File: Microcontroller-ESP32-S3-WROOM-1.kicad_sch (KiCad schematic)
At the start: 26 parts, among them Q1 BC817, Q2 BC817, U1 ESP32-S3-WROOM-1, U4 CP2102N-Axx-xQFN20

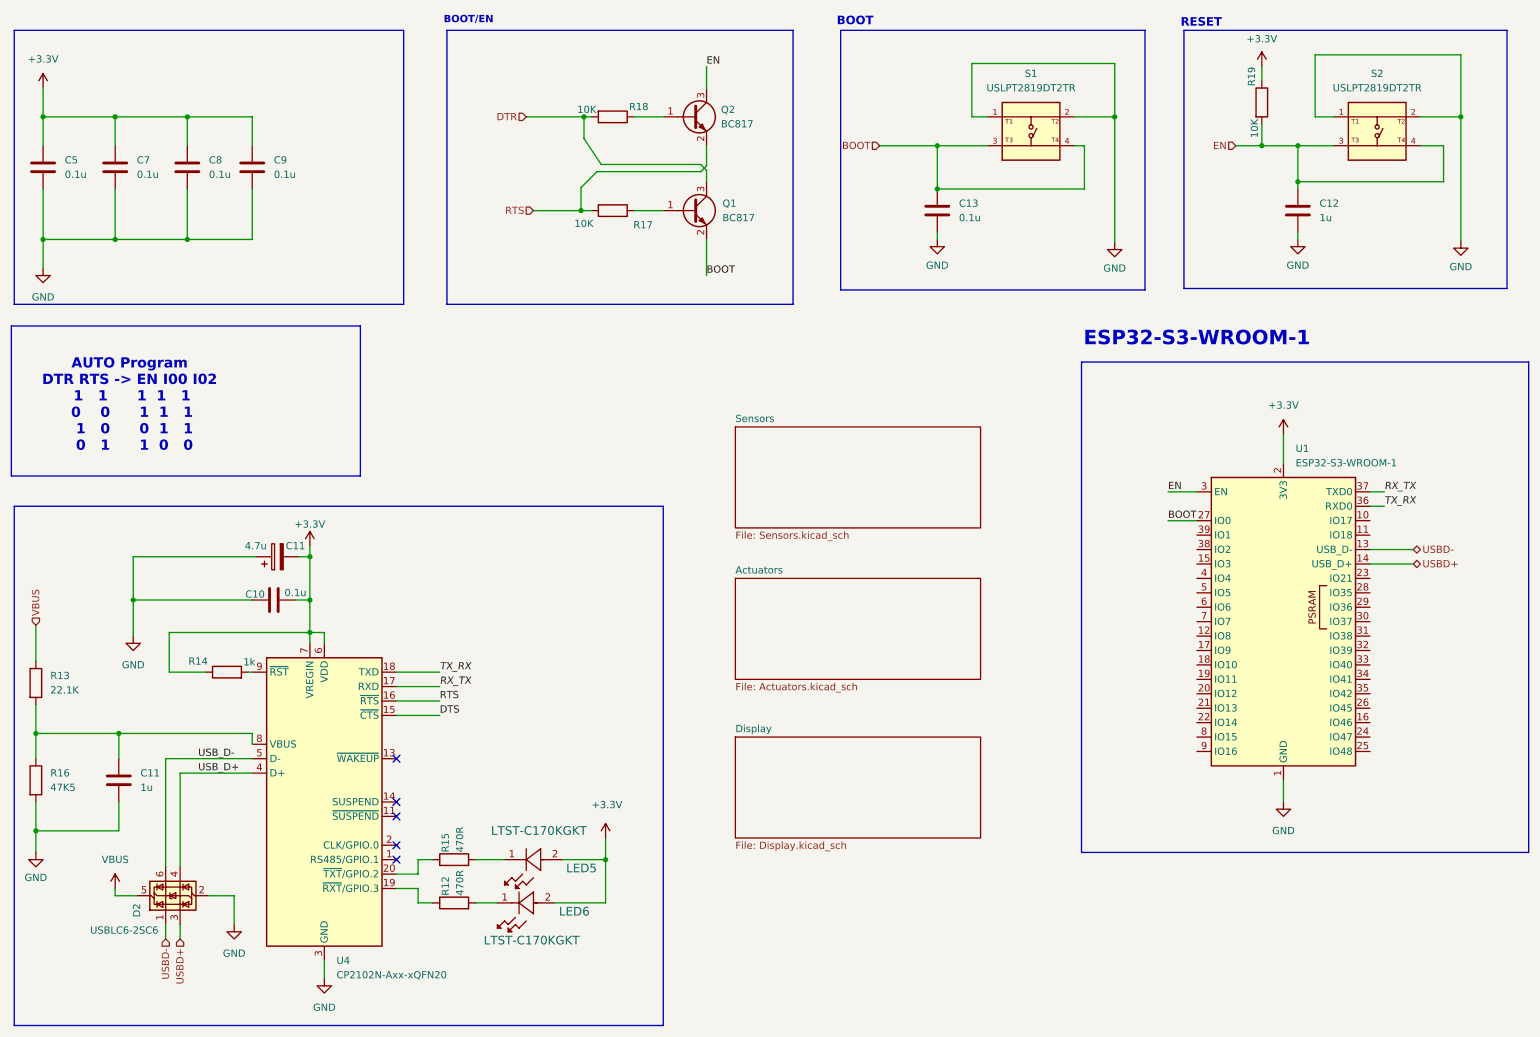
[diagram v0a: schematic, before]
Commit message: feat(hw): update component references for improved consistency in PCB design
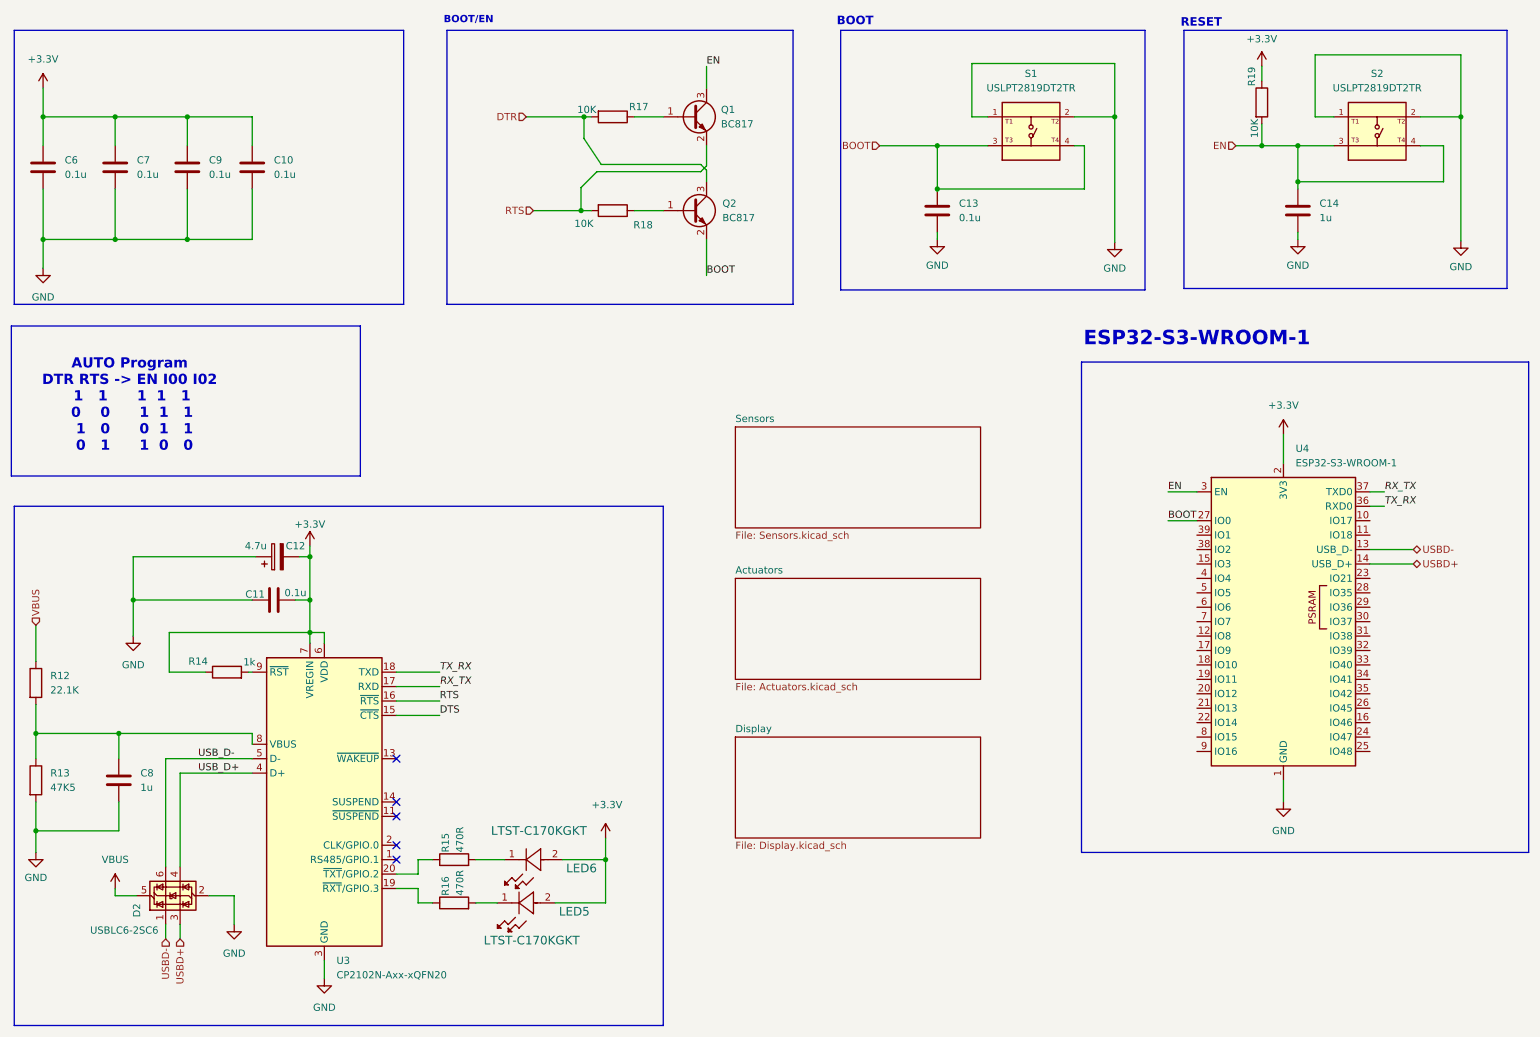
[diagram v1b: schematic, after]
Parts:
- renumbered C9 to C10, C10 to C11, C11 to C12, C12 to C14, C5 to C6, C11 to C8, C8 to C9, LED6 to LED5, LED5 to LED6, Q2 to Q1, Q1 to Q2, R13 to R12, R16 to R13, R12 to R16, R18 to R17, R17 to R18, U4 to U3, U1 to U4
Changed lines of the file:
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@@
 		(dnp no)
 		(fields_autoplaced yes)
-		(property "Reference" "Q1"
+		(property "Reference" "Q2"
 			(at 139.954 48.2599 0)
 			(effects
@@
 			(project "iot_device_pcb"
 				(path "/20a6db8f-6f9d-426b-a90e-3cd30ac36ee8/d76e5a61-e019-4441-8e0f-87cbb4ce42a5"
-					(reference "Q1")
+					(reference "Q2")
 					(unit 1)
 				)
@@
 		(dnp no)
 		(fields_autoplaced yes)
-		(property "Reference" "#PWR025"
+		(property "Reference" "#PWR039"
 			(at 238.76 92.71 0)
 			(effects
@@
 			(project ""
 				(path "/20a6db8f-6f9d-426b-a90e-3cd30ac36ee8/d76e5a61-e019-4441-8e0f-87cbb4ce42a5"
-					(reference "#PWR025")
+					(reference "#PWR039")
 					(unit 1)
 				)
@@
 		(dnp no)
 		(fields_autoplaced yes)
-		(property "Reference" "C9"
+		(property "Reference" "C10"
 			(at 60.96 40.6399 0)
 			(effects
@@
 			(project "iot_device_pcb"
 				(path "/20a6db8f-6f9d-426b-a90e-3cd30ac36ee8/d76e5a61-e019-4441-8e0f-87cbb4ce42a5"
-					(reference "C9")
+					(reference "C10")
 					(unit 1)
 				)
@@
 		(dnp no)
 		(fields_autoplaced yes)
-		(property "Reference" "#PWR0107"
+		(property "Reference" "#PWR036"
 			(at 177.8 60.96 0)
 			(effects
@@
 			(project "iot_device_pcb"
 				(path "/20a6db8f-6f9d-426b-a90e-3cd30ac36ee8/d76e5a61-e019-4441-8e0f-87cbb4ce42a5"
-					(reference "#PWR0107")
+					(reference "#PWR036")
 					(unit 1)
 				)
@@
 		(on_board yes)
 		(dnp no)
-		(property "Reference" "LED6"
+		(property "Reference" "LED5"
 			(at 116.586 172.974 0)
 			(effects
@@
 			(project "iot_device_pcb"
 				(path "/20a6db8f-6f9d-426b-a90e-3cd30ac36ee8/d76e5a61-e019-4441-8e0f-87cbb4ce42a5"
-					(reference "LED6")
+					(reference "LED5")
 					(unit 1)
 				)
@@
 		(dnp no)
 		(fields_autoplaced yes)
-		(property "Reference" "#PWR027"
+		(property "Reference" "#PWR028"
 			(at 20.32 31.75 0)
 			(effects
@@
 			(project "iot_device_pcb"
 				(path "/20a6db8f-6f9d-426b-a90e-3cd30ac36ee8/d76e5a61-e019-4441-8e0f-87cbb4ce42a5"
-					(reference "#PWR027")
+					(reference "#PWR028")
 					(unit 1)
 				)
@@
 		(dnp no)
 		(fields_autoplaced yes)
-		(property "Reference" "R13"
+		(property "Reference" "R12"
 			(at 21.59 131.4449 0)
 			(effects
@@
 			(project "iot_device_pcb"
 				(path "/20a6db8f-6f9d-426b-a90e-3cd30ac36ee8/d76e5a61-e019-4441-8e0f-87cbb4ce42a5"
-					(reference "R13")
+					(reference "R12")
 					(unit 1)
 				)
@@
 		(dnp no)
 		(fields_autoplaced yes)
-		(property "Reference" "C12"
+		(property "Reference" "C14"
 			(at 245.11 48.2599 0)
 			(effects
@@
 			(project "iot_device_pcb"
 				(path "/20a6db8f-6f9d-426b-a90e-3cd30ac36ee8/d76e5a61-e019-4441-8e0f-87cbb4ce42a5"
-					(reference "C12")
+					(reference "C14")
 					(unit 1)
 				)
@@
 		(dnp no)
 		(fields_autoplaced yes)
-		(property "Reference" "R16"
+		(property "Reference" "R13"
 			(at 21.59 148.5899 0)
 			(effects
@@
 			(project "iot_device_pcb"
 				(path "/20a6db8f-6f9d-426b-a90e-3cd30ac36ee8/d76e5a61-e019-4441-8e0f-87cbb4ce42a5"
-					(reference "R16")
+					(reference "R13")
 					(unit 1)
 				)
@@
 		(dnp no)
 		(fields_autoplaced yes)
-		(property "Reference" "#PWR0104"
+		(property "Reference" "#PWR041"
 			(at 241.3 60.96 0)
 			(effects
@@
 			(project "iot_device_pcb"
 				(path "/20a6db8f-6f9d-426b-a90e-3cd30ac36ee8/d76e5a61-e019-4441-8e0f-87cbb4ce42a5"
-					(reference "#PWR0104")
+					(reference "#PWR041")
 					(unit 1)
 				)
@@
 		(dnp no)
 		(fields_autoplaced yes)
-		(property "Reference" "U4"
+		(property "Reference" "U3"
 			(at 71.9933 181.61 0)
 			(effects
@@
 			(project "iot_device_pcb"
 				(path "/20a6db8f-6f9d-426b-a90e-3cd30ac36ee8/d76e5a61-e019-4441-8e0f-87cbb4ce42a5"
-					(reference "U4")
+					(reference "U3")
 					(unit 1)
 				)
@@
 		(on_board yes)
 		(dnp no)
-		(property "Reference" "R18"
+		(property "Reference" "R17"
 			(at 125.222 31.242 90)
 			(effects
@@
 			(project "iot_device_pcb"
 				(path "/20a6db8f-6f9d-426b-a90e-3cd30ac36ee8/d76e5a61-e019-4441-8e0f-87cbb4ce42a5"
-					(reference "R18")
+					(reference "R17")
 					(unit 1)
 				)
@@
 		(on_board yes)
 		(dnp no)
-		(property "Reference" "R17"
+		(property "Reference" "R18"
 			(at 125.984 52.07 90)
 			(effects
@@
 			(project "iot_device_pcb"
 				(path "/20a6db8f-6f9d-426b-a90e-3cd30ac36ee8/d76e5a61-e019-4441-8e0f-87cbb4ce42a5"
-					(reference "R17")
+					(reference "R18")
 					(unit 1)
 				)
@@
 		(on_board yes)
 		(dnp no)
-		(property "Reference" "LED5"
+		(property "Reference" "LED6"
 			(at 117.856 165.354 0)
 			(effects
@@
 			(project "iot_device_pcb"
 				(path "/20a6db8f-6f9d-426b-a90e-3cd30ac36ee8/d76e5a61-e019-4441-8e0f-87cbb4ce42a5"
-					(reference "LED5")
+					(reference "LED6")
 					(unit 1)
 				)
@@
 		(dnp no)
 		(fields_autoplaced yes)
-		(property "Reference" "U1"
+		(property "Reference" "U4"
 			(at 240.9033 91.44 0)
 			(effects
@@
 			(project ""
 				(path "/20a6db8f-6f9d-426b-a90e-3cd30ac36ee8/d76e5a61-e019-4441-8e0f-87cbb4ce42a5"
-					(reference "U1")
+					(reference "U4")
 					(unit 1)
 				)
@@
 		(dnp no)
 		(fields_autoplaced yes)
-		(property "Reference" "#PWR0106"
+		(property "Reference" "#PWR038"
 			(at 234.95 27.94 0)
 			(effects
@@
 			(project "iot_device_pcb"
 				(path "/20a6db8f-6f9d-426b-a90e-3cd30ac36ee8/d76e5a61-e019-4441-8e0f-87cbb4ce42a5"
-					(reference "#PWR0106")
+					(reference "#PWR038")
 					(unit 1)
 				)
@@
 		(dnp no)
 		(fields_autoplaced yes)
-		(property "Reference" "C5"
+		(property "Reference" "C6"
 			(at 24.13 40.6399 0)
 			(effects
@@
 			(project "iot_device_pcb"
 				(path "/20a6db8f-6f9d-426b-a90e-3cd30ac36ee8/d76e5a61-e019-4441-8e0f-87cbb4ce42a5"
-					(reference "C5")
+					(reference "C6")
 					(unit 1)
 				)
@@
 		(dnp no)
 		(fields_autoplaced yes)
-		(property "Reference" "#PWR028"
+		(property "Reference" "#PWR030"
 			(at 33.02 172.72 0)
 			(effects
@@
 			(project ""
 				(path "/20a6db8f-6f9d-426b-a90e-3cd30ac36ee8/d76e5a61-e019-4441-8e0f-87cbb4ce42a5"
-					(reference "#PWR028")
+					(reference "#PWR030")
 					(unit 1)
 				)
@@
 		(on_board yes)
 		(dnp no)
-		(property "Reference" "R12"
+		(property "Reference" "R16"
 			(at 91.186 170.18 0)
 			(effects
@@
 			(project "iot_device_pcb"
 				(path "/20a6db8f-6f9d-426b-a90e-3cd30ac36ee8/d76e5a61-e019-4441-8e0f-87cbb4ce42a5"
-					(reference "R12")
+					(reference "R16")
 					(unit 1)
 				)
@@
 		(dnp no)
 		(fields_autoplaced yes)
-		(property "Reference" "#PWR0105"
+		(property "Reference" "#PWR042"
 			(at 270.002 61.214 0)
 			(effects
@@
 			(project "iot_device_pcb"
 				(path "/20a6db8f-6f9d-426b-a90e-3cd30ac36ee8/d76e5a61-e019-4441-8e0f-87cbb4ce42a5"
-					(reference "#PWR0105")
+					(reference "#PWR042")
 					(unit 1)
 				)
@@
 		(dnp no)
 		(fields_autoplaced yes)
-		(property "Reference" "#PWR0103"
+		(property "Reference" "#PWR037"
 			(at 209.042 61.468 0)
 			(effects
@@
 			(project "iot_device_pcb"
 				(path "/20a6db8f-6f9d-426b-a90e-3cd30ac36ee8/d76e5a61-e019-4441-8e0f-87cbb4ce42a5"
-					(reference "#PWR0103")
+					(reference "#PWR037")
 					(unit 1)
 				)
@@
 		(dnp no)
 		(fields_autoplaced yes)
-		(property "Reference" "#PWR026"
+		(property "Reference" "#PWR029"
 			(at 20.32 66.04 0)
 			(effects
@@
 			(project "iot_device_pcb"
 				(path "/20a6db8f-6f9d-426b-a90e-3cd30ac36ee8/d76e5a61-e019-4441-8e0f-87cbb4ce42a5"
-					(reference "#PWR026")
+					(reference "#PWR029")
 					(unit 1)
 				)
@@
 		(on_board yes)
 		(dnp no)
-		(property "Reference" "C11"
+		(property "Reference" "C12"
 			(at 64.77 108.585 90)
 			(effects
@@
 			(project "iot_device_pcb"
 				(path "/20a6db8f-6f9d-426b-a90e-3cd30ac36ee8/d76e5a61-e019-4441-8e0f-87cbb4ce42a5"
-					(reference "C11")
+					(reference "C12")
 					(unit 1)
 				)
@@
 		(dnp no)
 		(fields_autoplaced yes)
-		(property "Reference" "Q2"
+		(property "Reference" "Q1"
 			(at 139.7 31.7499 0)
 			(effects
@@
 			(project "iot_device_pcb"
 				(path "/20a6db8f-6f9d-426b-a90e-3cd30ac36ee8/d76e5a61-e019-4441-8e0f-87cbb4ce42a5"
-					(reference "Q2")
+					(reference "Q1")
 					(unit 1)
 				)
@@
 		(on_board yes)
 		(dnp no)
-		(property "Reference" "C10"
+		(property "Reference" "C11"
 			(at 57.658 117.094 90)
 			(effects
@@
 			(project "iot_device_pcb"
 				(path "/20a6db8f-6f9d-426b-a90e-3cd30ac36ee8/d76e5a61-e019-4441-8e0f-87cbb4ce42a5"
-					(reference "C10")
+					(reference "C11")
 					(unit 1)
 				)
@@
 		(dnp no)
 		(fields_autoplaced yes)
-		(property "Reference" "#PWR024"
+		(property "Reference" "#PWR040"
 			(at 238.76 160.02 0)
 			(effects
@@
 			(project ""
 				(path "/20a6db8f-6f9d-426b-a90e-3cd30ac36ee8/d76e5a61-e019-4441-8e0f-87cbb4ce42a5"
-					(reference "#PWR024")
+					(reference "#PWR040")
 					(unit 1)
 				)
@@
 		(dnp no)
 		(fields_autoplaced yes)
-		(property "Reference" "#PWR030"
+		(property "Reference" "#PWR027"
 			(at 19.05 168.91 0)
 			(effects
@@
 			(project "iot_device_pcb"
 				(path "/20a6db8f-6f9d-426b-a90e-3cd30ac36ee8/d76e5a61-e019-4441-8e0f-87cbb4ce42a5"
-					(reference "#PWR030")
+					(reference "#PWR027")
 					(unit 1)
 				)
@@
 		(dnp no)
 		(fields_autoplaced yes)
-		(property "Reference" "C8"
+		(property "Reference" "C9"
 			(at 49.53 40.6399 0)
 			(effects
@@
 			(project "iot_device_pcb"
 				(path "/20a6db8f-6f9d-426b-a90e-3cd30ac36ee8/d76e5a61-e019-4441-8e0f-87cbb4ce42a5"
-					(reference "C8")
+					(reference "C9")
 					(unit 1)
 				)
@@
 		(dnp no)
 		(fields_autoplaced yes)
-		(property "Reference" "C11"
+		(property "Reference" "C8"
 			(at 37.465 148.5899 0)
 			(effects
@@
 			(project "iot_device_pcb"
 				(path "/20a6db8f-6f9d-426b-a90e-3cd30ac36ee8/d76e5a61-e019-4441-8e0f-87cbb4ce42a5"
-					(reference "C11")
+					(reference "C8")
 					(unit 1)
 				)
